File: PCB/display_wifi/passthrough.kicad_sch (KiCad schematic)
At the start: 4 parts, among them J5 694106301002, J6 Conn_ST_STDC14, J7 53261-0671, J8 53261-0671

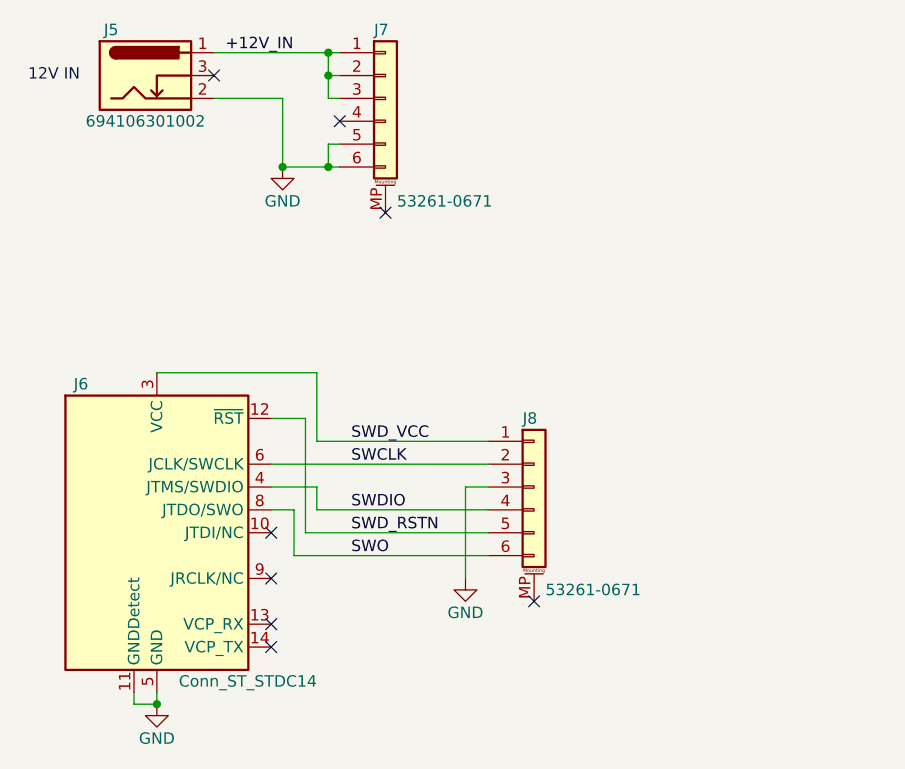
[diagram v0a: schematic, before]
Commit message: Added part numbers for cables
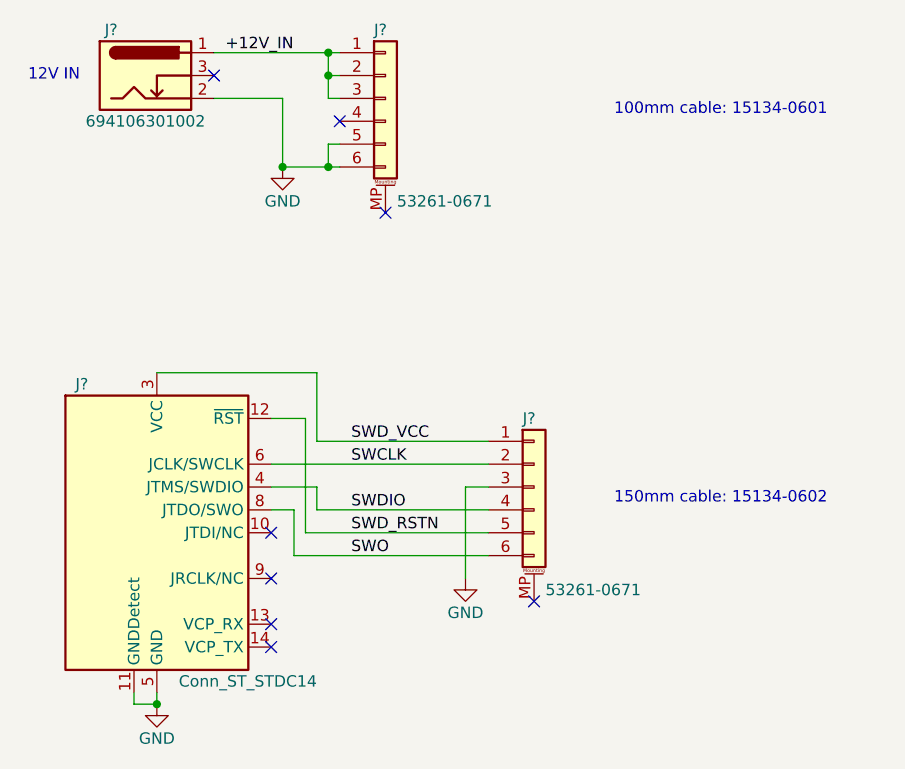
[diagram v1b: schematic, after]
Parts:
- renumbered J8 to J?, J5 to J?, J6 to J?, J7 to J?
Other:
- note added: "100mm cable: 15134-0601"
- note added: "150mm cable: 15134-0602"
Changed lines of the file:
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@@
 	(generator_version "9.0")
 	(paper "A4")
+	(text "100mm cable: 15134-0601"
+		(exclude_from_sim no)
+		(at 166.37 59.69 0)
+		(effects
+			(font
+				(size 1.27 1.27)
+			)
+			(justify left)
+		)
+	)
 	(text "12V IN"
 		(exclude_from_sim no)
@@
 				(size 1.27 1.27)
 			)
+		)
+	)
+	(text "150mm cable: 15134-0602"
+		(exclude_from_sim no)
+		(at 166.37 102.87 0)
+		(effects
+			(font
+				(size 1.27 1.27)
+			)
+			(justify left)
 		)
 	)
@@
 		(on_board yes)
 		(dnp no)
-		(property "Reference" "#PWR032"
+		(property "Reference" "#PWR?"
 			(at 115.57 132.08 0)
 			(effects
@@
 		)
 		(instances
+			(project "passthrough"
+				(path "/4748efed-0c83-4e53-b6e4-29f8b0fa78f5"
+					(reference "#PWR?")
+					(unit 1)
+				)
+			)
 			(project "display_wifi"
 				(path "/c8a7c37e-85db-4c80-9732-f9406c6cc5f6/e7bb56ec-bae5-49e7-bcf6-d179aa1ca995"
@@
 		(on_board yes)
 		(dnp no)
-		(property "Reference" "J8"
+		(property "Reference" "J?"
 			(at 156.21 93.98 0)
 			(effects
@@
 		)
 		(instances
+			(project "passthrough"
+				(path "/4748efed-0c83-4e53-b6e4-29f8b0fa78f5"
+					(reference "J?")
+					(unit 1)
+				)
+			)
 			(project "display_wifi"
 				(path "/c8a7c37e-85db-4c80-9732-f9406c6cc5f6/e7bb56ec-bae5-49e7-bcf6-d179aa1ca995"
@@
 		(on_board yes)
 		(dnp no)
-		(property "Reference" "J5"
+		(property "Reference" "J?"
 			(at 110.49 50.8 0)
 			(effects
@@
 		)
 		(instances
+			(project "passthrough"
+				(path "/4748efed-0c83-4e53-b6e4-29f8b0fa78f5"
+					(reference "J?")
+					(unit 1)
+				)
+			)
 			(project "display_wifi"
 				(path "/c8a7c37e-85db-4c80-9732-f9406c6cc5f6/e7bb56ec-bae5-49e7-bcf6-d179aa1ca995"
@@
 		(on_board yes)
 		(dnp no)
-		(property "Reference" "#PWR033"
+		(property "Reference" "#PWR?"
 			(at 129.54 72.39 0)
 			(effects
@@
 		)
 		(instances
+			(project "passthrough"
+				(path "/4748efed-0c83-4e53-b6e4-29f8b0fa78f5"
+					(reference "#PWR?")
+					(unit 1)
+				)
+			)
 			(project "display_wifi"
 				(path "/c8a7c37e-85db-4c80-9732-f9406c6cc5f6/e7bb56ec-bae5-49e7-bcf6-d179aa1ca995"
@@
 		(on_board yes)
 		(dnp no)
-		(property "Reference" "J6"
+		(property "Reference" "J?"
 			(at 107.95 90.17 0)
 			(effects
@@
 		)
 		(instances
+			(project "passthrough"
+				(path "/4748efed-0c83-4e53-b6e4-29f8b0fa78f5"
+					(reference "J?")
+					(unit 1)
+				)
+			)
 			(project "display_wifi"
 				(path "/c8a7c37e-85db-4c80-9732-f9406c6cc5f6/e7bb56ec-bae5-49e7-bcf6-d179aa1ca995"
@@
 		(on_board yes)
 		(dnp no)
-		(property "Reference" "J7"
+		(property "Reference" "J?"
 			(at 139.7 50.8 0)
 			(effects
@@
 		)
 		(instances
+			(project "passthrough"
+				(path "/4748efed-0c83-4e53-b6e4-29f8b0fa78f5"
+					(reference "J?")
+					(unit 1)
+				)
+			)
 			(project "display_wifi"
 				(path "/c8a7c37e-85db-4c80-9732-f9406c6cc5f6/e7bb56ec-bae5-49e7-bcf6-d179aa1ca995"
@@
 		(on_board yes)
 		(dnp no)
-		(property "Reference" "#PWR034"
+		(property "Reference" "#PWR?"
 			(at 149.86 118.11 0)
 			(effects
@@
 		)
 		(instances
+			(project "passthrough"
+				(path "/4748efed-0c83-4e53-b6e4-29f8b0fa78f5"
+					(reference "#PWR?")
+					(unit 1)
+				)
+			)
 			(project "display_wifi"
 				(path "/c8a7c37e-85db-4c80-9732-f9406c6cc5f6/e7bb56ec-bae5-49e7-bcf6-d179aa1ca995"
@@
 		)
 	)
+	(sheet_instances
+		(path "/"
+			(page "1")
+		)
+	)
+	(embedded_fonts no)
 )

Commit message: Updated PCB to v1.1
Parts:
- gave numbers to parts that had none: 4
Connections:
- net DEBUG_TXD: now reaches J6.14 (VCP_TX)
- no-connect marks 8 -> 7
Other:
- note added: "50mm cable: 15134-0600"
- note added: "Needs pin direction swap"
- note removed: "150mm cable: 15134-0602"
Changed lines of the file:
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@@
 	(generator_version "9.0")
 	(paper "A4")
+	(title_block
+		(date "2025-11-26")
+		(rev "1.10")
+	)
+	(text "50mm cable: 15134-0600"
+		(exclude_from_sim no)
+		(at 165.1 58.42 0)
+		(effects
+			(font
+				(size 1.27 1.27)
+			)
+			(justify left)
+		)
+	)
+	(text "Needs pin direction swap"
+		(exclude_from_sim no)
+		(at 165.1 104.14 0)
+		(effects
+			(font
+				(size 1.27 1.27)
+			)
+			(justify left)
+		)
+	)
 	(text "100mm cable: 15134-0601"
 		(exclude_from_sim no)
-		(at 166.37 59.69 0)
+		(at 165.1 101.6 0)
 		(effects
 			(font
@@
 		)
 	)
-	(text "150mm cable: 15134-0602"
-		(exclude_from_sim no)
-		(at 166.37 102.87 0)
+	(text "Needs pin direction swap"
+		(exclude_from_sim no)
+		(at 165.1 60.96 0)
 		(effects
 			(font
@@
 	)
 	(no_connect
-		(at 128.27 119.38)
-	)
-	(no_connect
 		(at 157.48 114.3)
 	)
@@
 		)
 	)
+	(wire
+		(pts
+			(xy 129.54 119.38) (xy 128.27 119.38)
+		)
+		(stroke
+			(width 0)
+			(type default)
+		)
+	)
 	(label "SWO"
 		(at 137.16 109.22 0)
@@
 			)
 			(justify left bottom)
+		)
+	)
+	(global_label "DEBUG_TXD"
+		(shape input)
+		(at 129.54 119.38 0)
+		(fields_autoplaced yes)
+		(effects
+			(font
+				(size 1.27 1.27)
+			)
+			(justify left)
+		)
+		(property "Intersheetrefs" "${INTERSHEET_REFS}"
+			(at 143.2294 119.38 0)
+			(effects
+				(font
+					(size 1.27 1.27)
+				)
+				(justify left)
+				(hide yes)
+			)
 		)
 	)
@@
 		(on_board yes)
 		(dnp no)
-		(property "Reference" "#PWR?"
+		(property "Reference" "#PWR032"
 			(at 115.57 132.08 0)
 			(effects
@@
 		(on_board yes)
 		(dnp no)
-		(property "Reference" "J?"
+		(property "Reference" "J8"
 			(at 156.21 93.98 0)
 			(effects
@@
 		(on_board yes)
 		(dnp no)
-		(property "Reference" "J?"
+		(property "Reference" "J5"
 			(at 110.49 50.8 0)
 			(effects
@@
 		(on_board yes)
 		(dnp no)
-		(property "Reference" "#PWR?"
+		(property "Reference" "#PWR033"
 			(at 129.54 72.39 0)
 			(effects
@@
 		(on_board yes)
 		(dnp no)
-		(property "Reference" "J?"
+		(property "Reference" "J6"
 			(at 107.95 90.17 0)
 			(effects
@@
 		(on_board yes)
 		(dnp no)
-		(property "Reference" "J?"
+		(property "Reference" "J7"
 			(at 139.7 50.8 0)
 			(effects
@@
 		(on_board yes)
 		(dnp no)
-		(property "Reference" "#PWR?"
+		(property "Reference" "#PWR034"
 			(at 149.86 118.11 0)
 			(effects
